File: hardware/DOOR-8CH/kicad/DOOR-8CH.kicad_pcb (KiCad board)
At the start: 4 copper layers, 260 x 160 mm, 230 parts, among them J1 FUSED_12V_CH1, J10 ACTUATOR_CH2, J11 ACTUATOR_CH3, J12 ACTUATOR_CH4, J13 ACTUATOR_CH5, J14 ACTUATOR_CH6, J15 ACTUATOR_CH7, J16 ACTUATOR_CH8, J2 FUSED_12V_CH2, J201 REED_A_OPEN_3V3_SIG_GND, J202 REED_A_CLOSED_3V3_SIG_GND, J203 REED_A_IN_PLACE_3V3_SIG_GND, J204 REED_B_OPEN_3V3_SIG_GND, J205 REED_B_CLOSED_3V3_SIG_GND, J206 REED_B_IN_PLACE_3V3_SIG_GND, J211 CAP_CS1_GND, J212 CAP_CS2_GND, J213 CAP_CS3_GND, J214 CAP_CS4_GND, J215 CAP_CS5_GND, J216 CAP_CS6_GND, J217 CAP_CS7_GND, J218 CAP_CS8_GND, J220 SWD_S1_3V3_DIO_CLK_NRST_GND, J230 LOGIC_12V_GND, J240 CANH_CANL_GND_SHIELD, J3 FUSED_12V_CH3, J4 FUSED_12V_CH4, J5 FUSED_12V_CH5, J6 FUSED_12V_CH6, J7 FUSED_12V_CH7, J8 FUSED_12V_CH8, J9 ACTUATOR_CH1, U1 VNH5019A-E, U2 VNH5019A-E, U230 AMS1117-3V3, U250 25LC256_SOIC8_CARRIER_ID, U3 VNH5019A-E, U4 VNH5019A-E, U5 VNH5019A-E, U6 VNH5019A-E, U7 VNH5019A-E, U8 VNH5019A-E

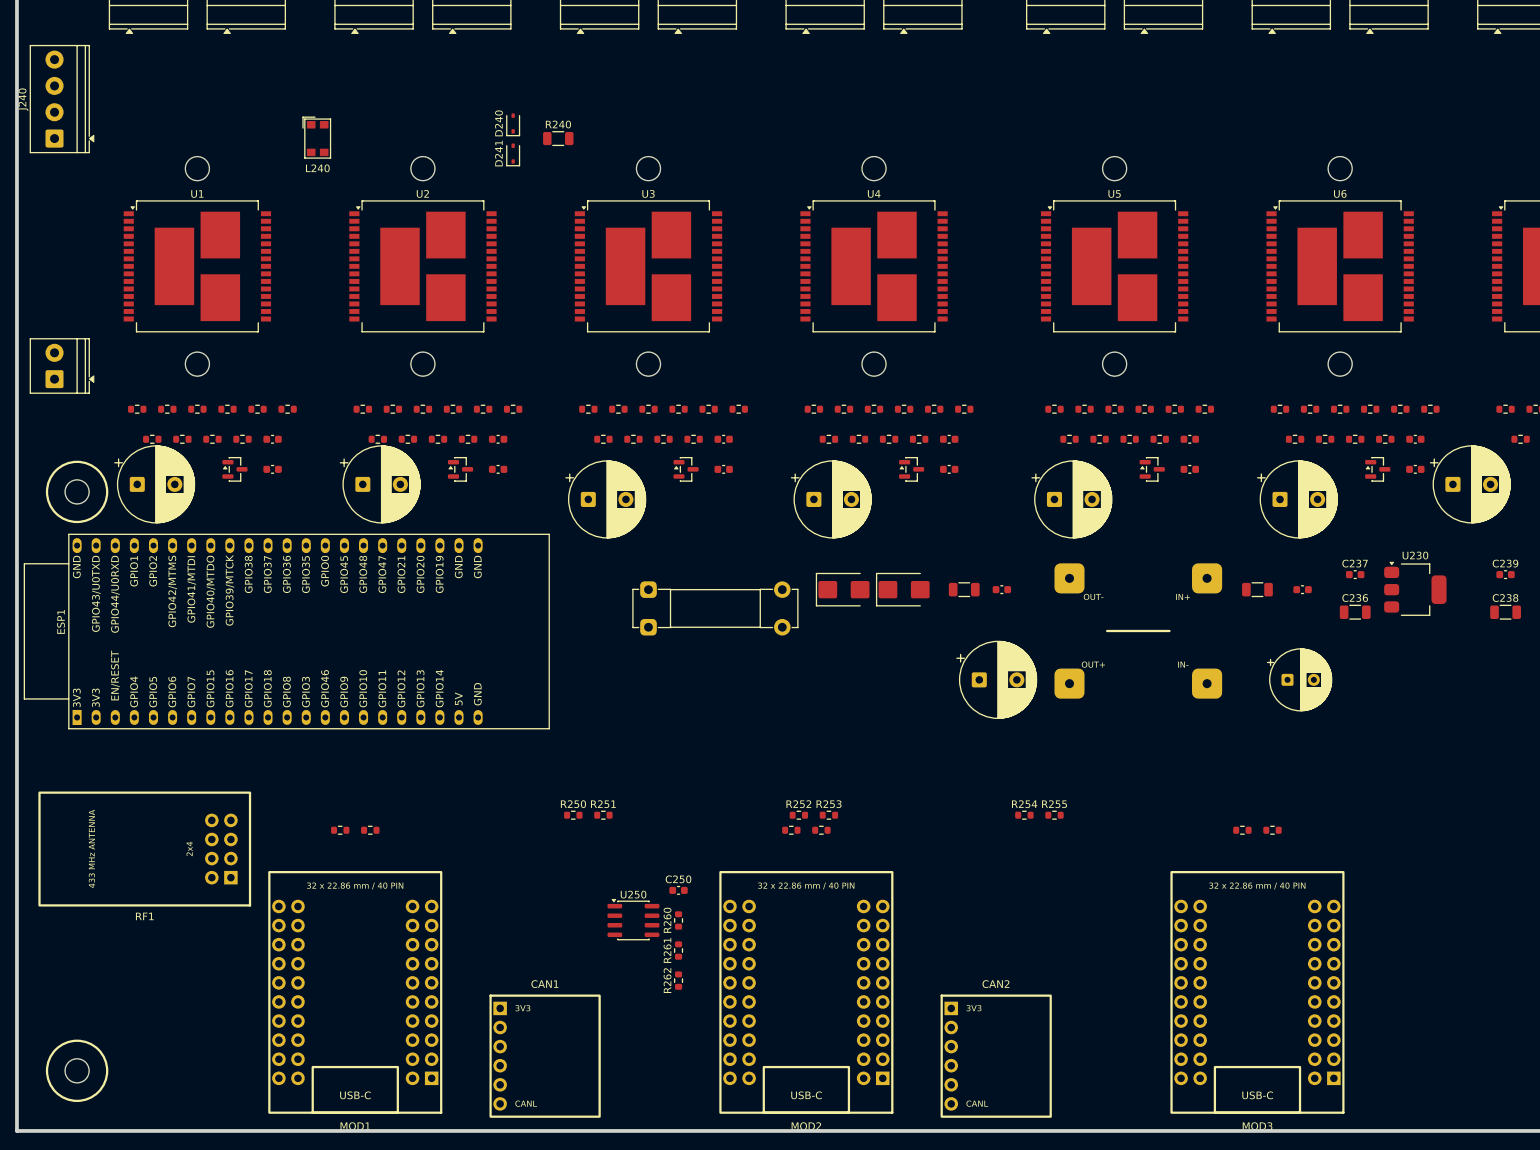
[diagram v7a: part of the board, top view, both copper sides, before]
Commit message: Move CAN entry next to CAN2
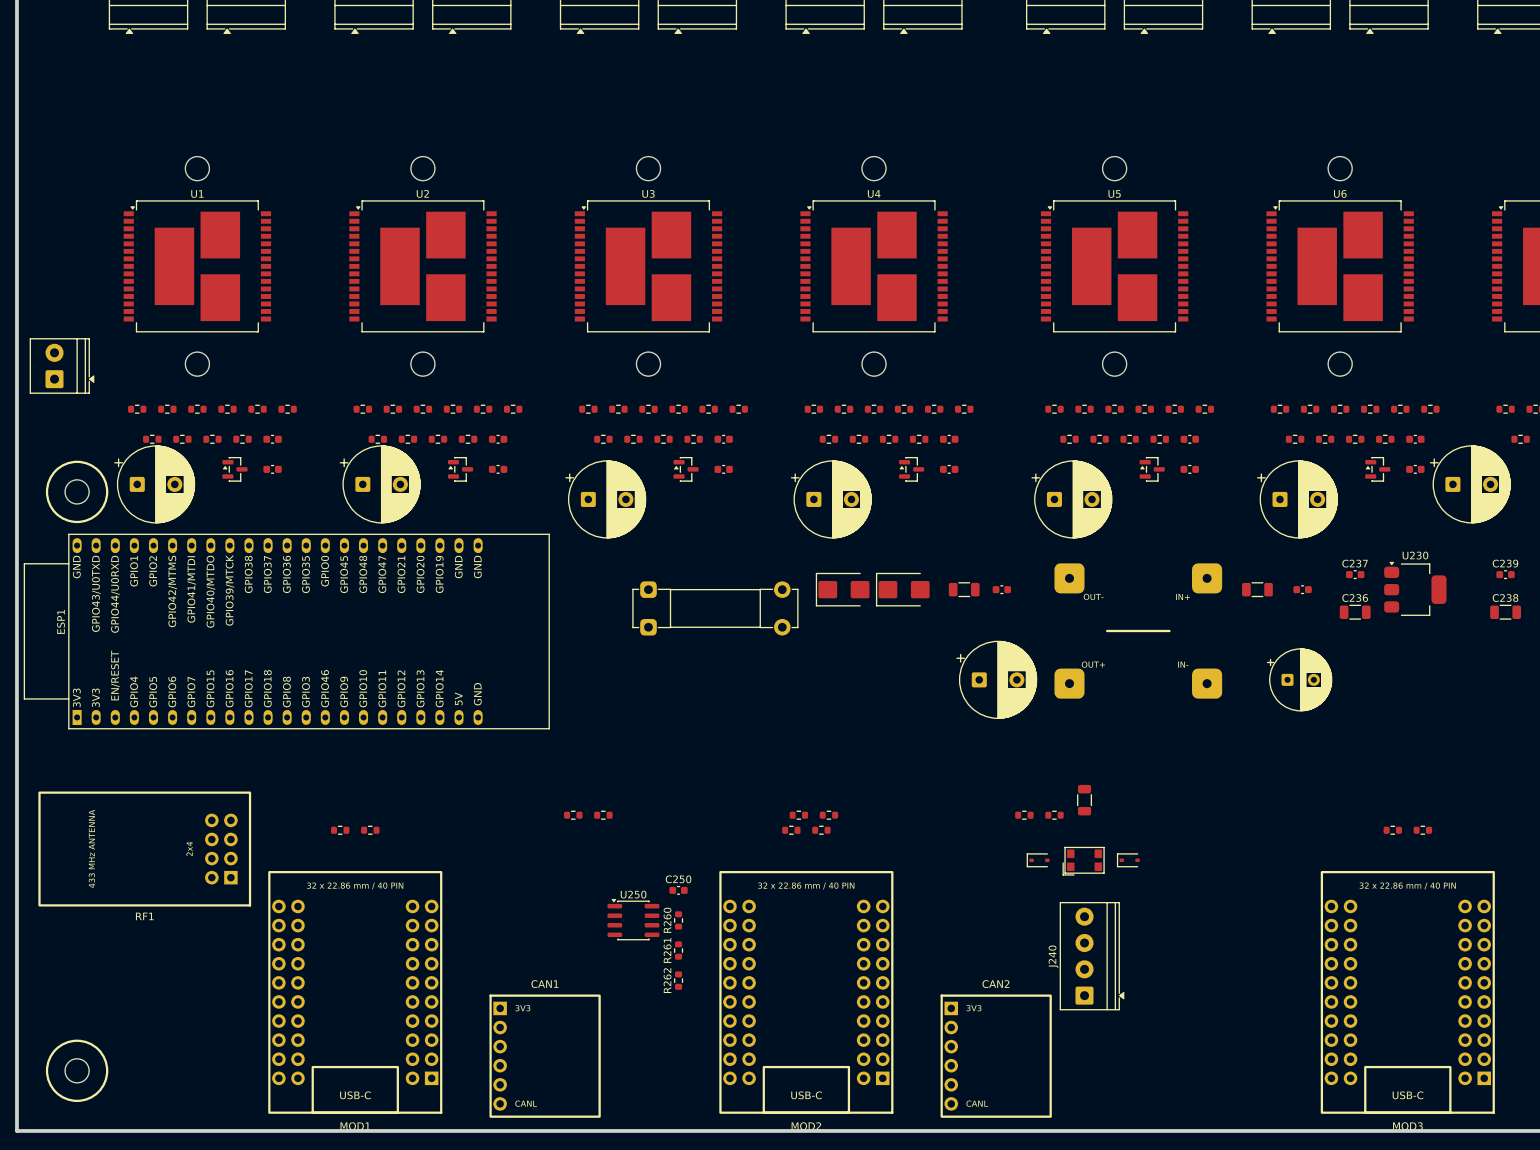
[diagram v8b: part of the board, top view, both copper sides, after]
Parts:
- moved J240 178.2 mm to (142.0, 142.0)
- moved L240 140.1 mm to (142.0, 124.0), turned to 90 degrees
- moved D241 124.7 mm to (148.0, 124.0), turned to 0 degrees
- moved D240 120.4 mm to (136.0, 124.0), turned to 0 degrees
- moved R240 112.4 mm to (142.0, 116.0), turned to 90 degrees
- moved MOD3 20.0 mm to (195.2, 153.0)
- moved R3031 20.0 mm to (183.0, 120.0)
- moved R3032 20.0 mm to (187.0, 120.0)
